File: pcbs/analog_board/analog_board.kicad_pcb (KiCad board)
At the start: 2 copper layers, 80 x 50 mm, 48 parts, among them P1 CONN_01X04, P2 CONN_01X03, P3 CONN_01X03, P4 CONN_01X03, P5 CONN_01X03, P6 CONN_01X03, P7 CONN_01X03, Q1 MMBT3904, U1 AD8616, U2 AD8616

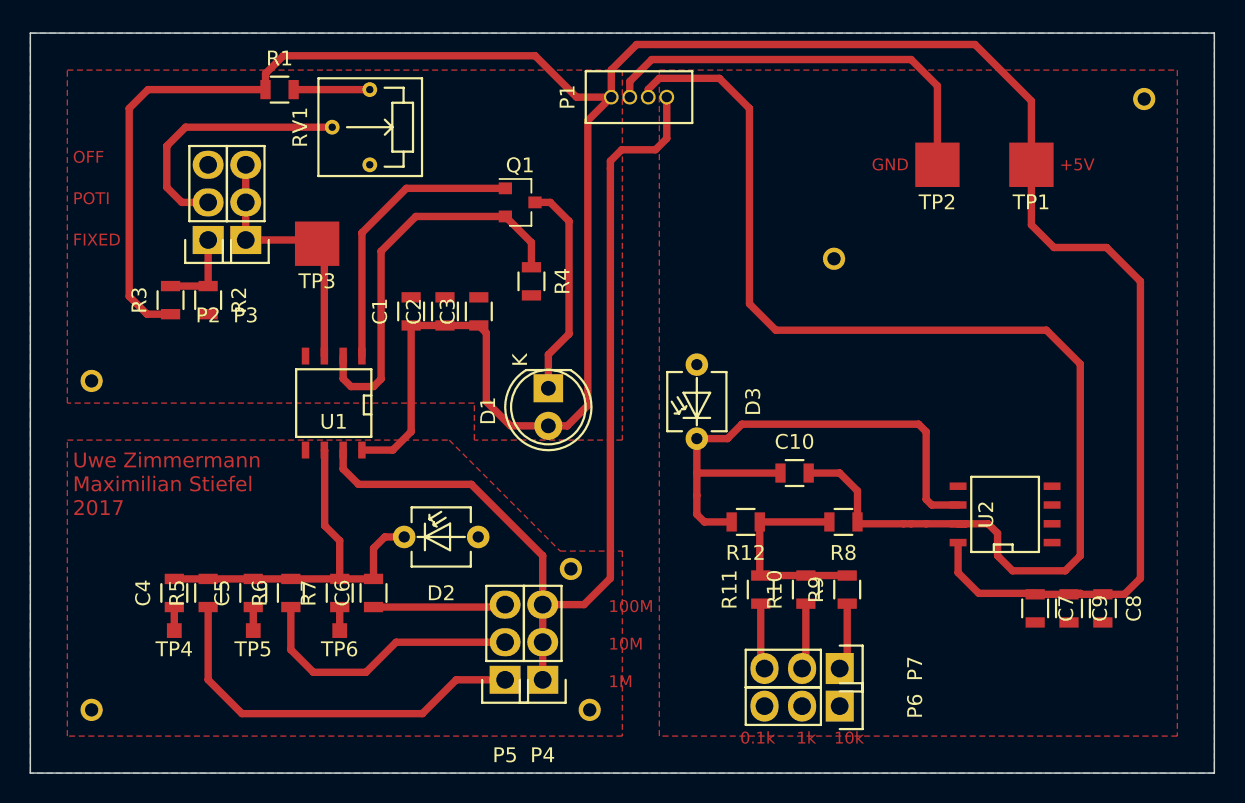
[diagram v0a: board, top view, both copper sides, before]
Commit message: Added some mounting holes.
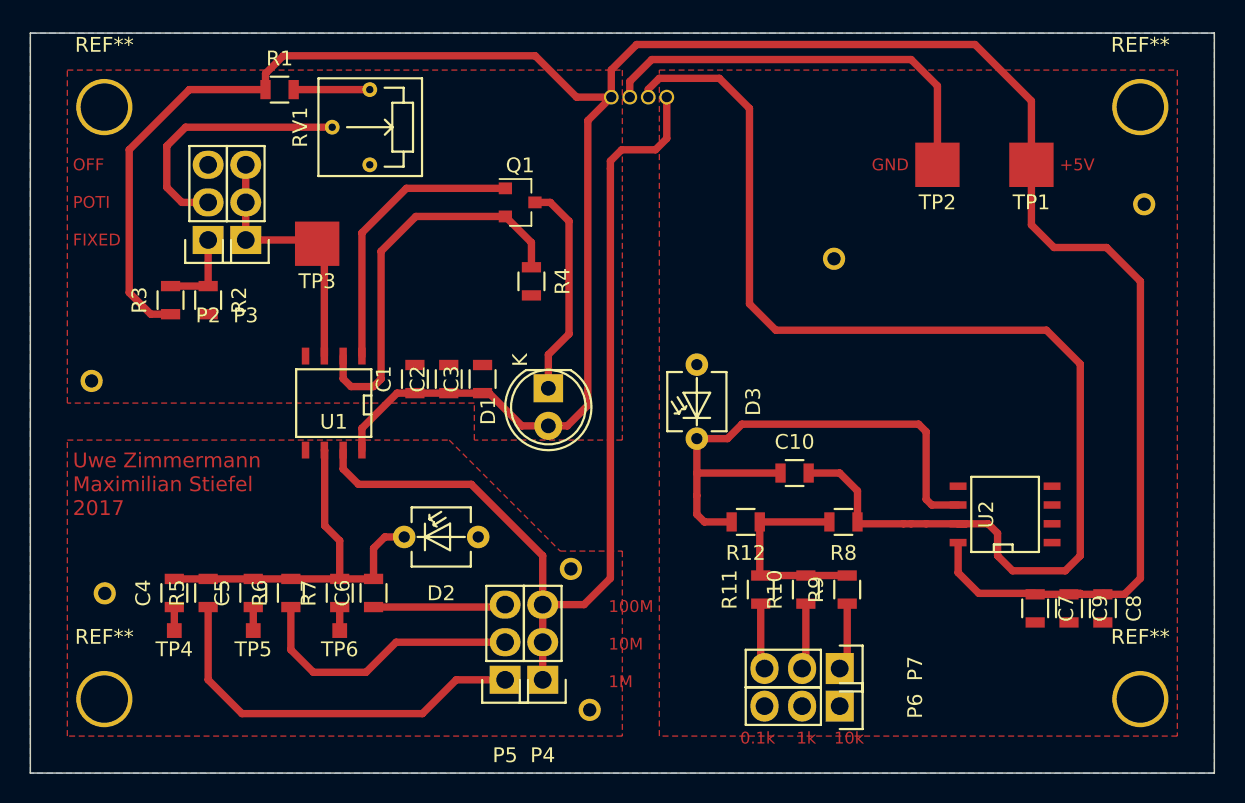
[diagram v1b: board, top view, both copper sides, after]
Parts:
- removed the REF** at (175.3, 84.5)
- removed the REF** at (104.1, 125.7)
- added REF**: Stitching-Via-0.8-1.5, Vias:Stitchging-Via-0.8-1.5, F.Cu at (105.0, 117.9)
- added REF**: MountingHole_3.2mm_M3, Mounting Holes:MountingHole_3.2mm_M3, F.Cu at (175.0, 125.0)
- added REF**: Stitching-Via-0.8-1.5, Vias:Stitchging-Via-0.8-1.5, F.Cu at (175.3, 91.6)
- added REF**: MountingHole_3.2mm_M3, Mounting Holes:MountingHole_3.2mm_M3, F.Cu at (105.0, 85.0)
- added REF**: MountingHole_3.2mm_M3, Mounting Holes:MountingHole_3.2mm_M3, F.Cu at (105.0, 125.0)
- added REF**: MountingHole_3.2mm_M3, Mounting Holes:MountingHole_3.2mm_M3, F.Cu at (175.0, 85.0)
- P1: moved to B.Cu
- moved C2 4.58 mm to (128.3, 103.4)
- moved C3 4.58 mm to (130.6, 103.4)
- moved C1 4.58 mm to (126.0, 103.4)
- turned P1 to 90 degrees
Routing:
- net +5V: track 188.0 -> 176.4 mm

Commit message: Almost done with the etching machine CAD work.
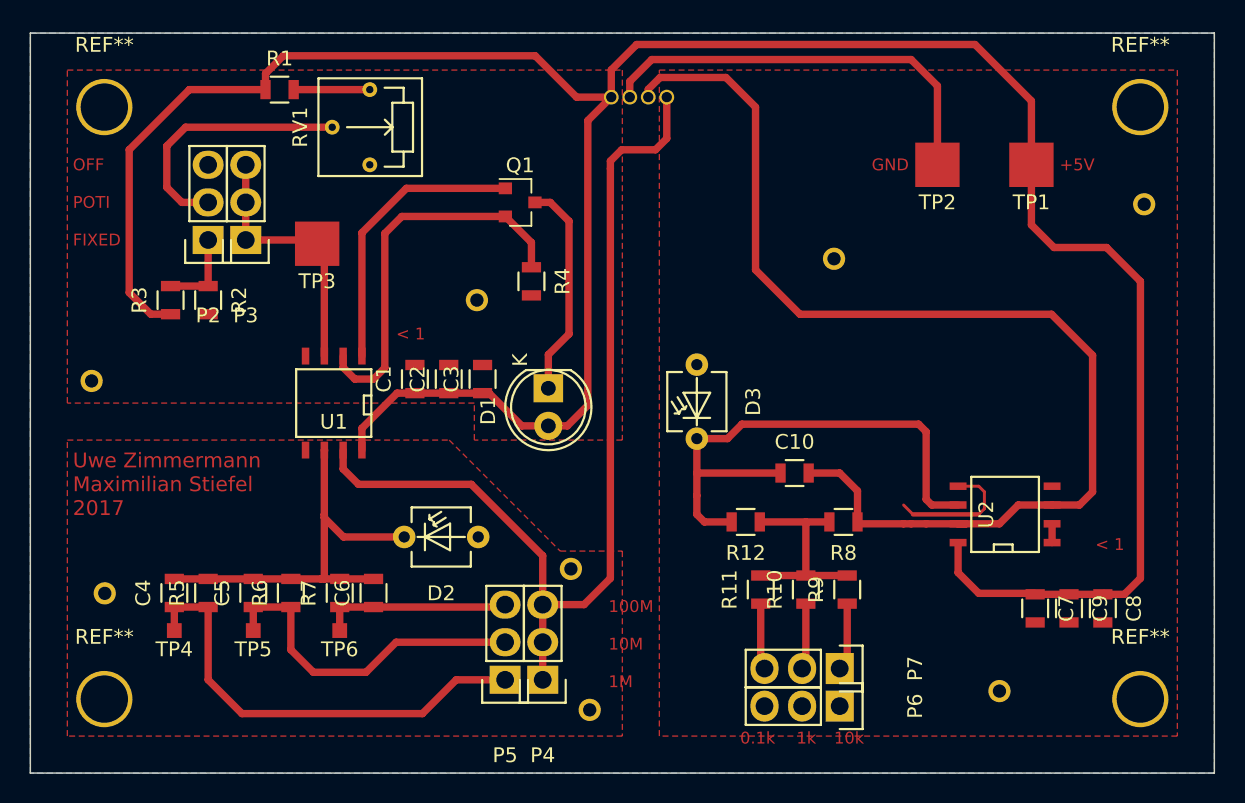
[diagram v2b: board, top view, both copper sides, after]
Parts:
- added REF**: Stitching-Via-0.8-1.5, Vias:Stitchging-Via-0.8-1.5, F.Cu at (130.2, 98.0)
- added REF**: Stitching-Via-0.8-1.5, Vias:Stitchging-Via-0.8-1.5, F.Cu at (165.5, 124.5)
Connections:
- U2 pad 1: (no net) -> Net-(U2-Pad1)
- U2 pad 2: (no net) -> Net-(U2-Pad1)
- U2 pad 3: (no net) -> /lowCurrent/BPW34FA_OUT
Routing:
- net GND: track 28.5 -> 37.5 mm
- net /lowCurrent/BPW34FA_OUT: track 83.4 -> 78.1 mm
- net Net-(C5-Pad1): track 20.4 -> 23.0 mm
- net Net-(C6-Pad1): track 10.5 -> 12.8 mm
- net Net-(C4-Pad1): track 28.5 -> 30.8 mm
- net Net-(C4-Pad2): track 27.1 -> 28.4 mm
- net Net-(U2-Pad1): track 0.00 -> 1.27 mm
- net Net-(Q1-Pad2): track 26.7 -> 26.1 mm
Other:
- board text added: "< 1"
